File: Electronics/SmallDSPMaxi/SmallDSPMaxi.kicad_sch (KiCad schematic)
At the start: 103 parts, among them J1 Header, J10 Header, J11 Programming, J2 Header, J3 Header, J4 Header, J5 Header, J6 Header, J7 Header, J8 Header, J9 Header, Q1 NSS1C300ET4G, SW1 SW_4PDT, SW2 TS-1187A-B-A-B, U1 ADAU1467, U2 ADM811, U3 M95M01-R, Y1 830105957509

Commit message: Adds final state of Maxi rev 1.0 and unbalanced IO boards rev 1.0.
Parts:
- removed D1, D10, D11, D12, D2, D3, D4, D5, D6, D7, D8, D9: P6SMB6.8CA, Diode_SMD:D_SMB, symbol Device:D_TVS
- added JP1: SolderJumper_2_Open, Jumper:SolderJumper-2_P1.3mm_Open_RoundedPad1.0x1.5mm, symbol Jumper:SolderJumper_2_Open
- added TP?: TestPoint, TestPoint:TestPoint_Pad_D1.0mm, symbol Connector:TestPoint_Small
- added U1, U3, U4: H5VU25U, Package_DFN_QFN:Diodes_UDFN-10_1.0x2.5mm_P0.5mm, symbol 1_Project_Symbols:H5VU25U
- U2: renamed from U1; Part Number ADAU1463 -> ADAU1467WBCPZ300
- Y1: Assembling (none) -> X
- renumbered C2 to C1, C1 to C2, C4 to C3, C5 to C4, C7 to C5, C8 to C6, C6 to C7, C3 to C8, D13 to D1, J9 to J10, J10 to J11, J11 to J7, J7 to J8, J8 to J9, R38 to R28, R33 to R32, R34 to R33, R28 to R34, R32 to R38, U1 to U2, U3 to U5, U2 to U6
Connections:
- net 5V PR: now also U3.4
- net Earth_Protective: now also U1.3 (VSS), U1.8 (VSS), U3.3 (VSS), U3.8 (VSS), U4.3 (VSS), U4.8 (VSS)
- net MCU SCL: now also U1.1
- net MCU SDA: now also U1.2
- net PRGM MISO: now also U3.5
- net PRGM MOSI: now also U4.2
- net PRGM SCLK: now also U3.2
- net ~{DSP RST}: now also JP1.2 (B)
- net ~{PRGM CS}: now also U3.1
- net at C2.1, R34.1, SW2.2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: now also JP1.1 (A), TP?.1, U4.4
- net at SW1.5 (B), TP?.1, U2.39 (S_SCL/S_SCLK): now also U1.4
- net at SW1.11 (B), U2.42 (Selfboot): now also U4.5
- net at SW1.2 (B), TP?.1, U2.38 (S_SDA/S_MISO): now also U1.5
- net BCLK In0 renamed DSP BCLK In 1
- net BCLK In1 renamed DSP BCLK In 2
- net BCLK In2 renamed DSP BCLK In 3
- net BCLK In3 renamed DSP BCLK In 4
- net BCLK Out0 renamed DSP BCLK Out 1
- net BCLK Out1 renamed DSP BCLK Out 2
- net BCLK Out2 renamed DSP BCLK Out 3
- net BCLK Out3 renamed DSP BCLK Out 4
- net GPIO14 renamed DSP GPIO14
- net GPIO15 renamed DSP GPIO15
- net GPIO6 renamed DSP GPIO6
- net GPIO7 renamed DSP GPIO7
- net LRCK In0 renamed DSP LRCK In 1
- net LRCK In1 renamed DSP LRCK In 2
- net LRCK In2 renamed DSP LRCK In 3
- net LRCK In3 renamed DSP LRCK In 4
- net LRCK Out0 renamed DSP LRCK Out 1
- net LRCK Out1 renamed DSP LRCK Out 2
- net LRCK Out2 renamed DSP LRCK Out 3
- net LRCK Out3 renamed DSP LRCK Out 4
- net M DSP MISO renamed DSP MISO
- net M DSP MOSI renamed DSP MOSI
- net M DSP SCLK renamed DSP SCLK
- net MCLK renamed DSP MCLK
- net SDATA In0 renamed DSP I²S SDI 1
- net SDATA In1 renamed DSP I²S SDI 2
- net SDATA In2 renamed DSP I²S SDI 3
- net SDATA In3 renamed DSP I²S SDI 4
- net SDATA In4 renamed DSP I²S SDI 5
- net SDATA In5 renamed DSP I²S SDI 6
- net SDATA In6 renamed DSP I²S SDI 7
- net SDATA In7 renamed DSP I²S SDI 8
- net SDATA Out0 renamed DSP I²S SDO 1
- net SDATA Out1 renamed DSP I²S SDO 2
- net SDATA Out2 renamed DSP I²S SDO 3
- net SDATA Out3 renamed DSP I²S SDO 4
- net SDATA Out4 renamed DSP I²S SDO 5
- net SDATA Out5 renamed DSP I²S SDO 6
- net SDATA Out6 renamed DSP I²S SDO 7
- net SDATA Out7 renamed DSP I²S SDO 8
- net ~{RST MCU} renamed ~{DSP RST MCU}
- net ~{RST PGRM} renamed ~{DSP RST PGRM}
- net ~{DSP RST PGRM}: now also U4.1
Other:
- moved on the sheet: C1, C2, C3, C4, C5, C6, C7, C8, C9, D1, J1, J10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

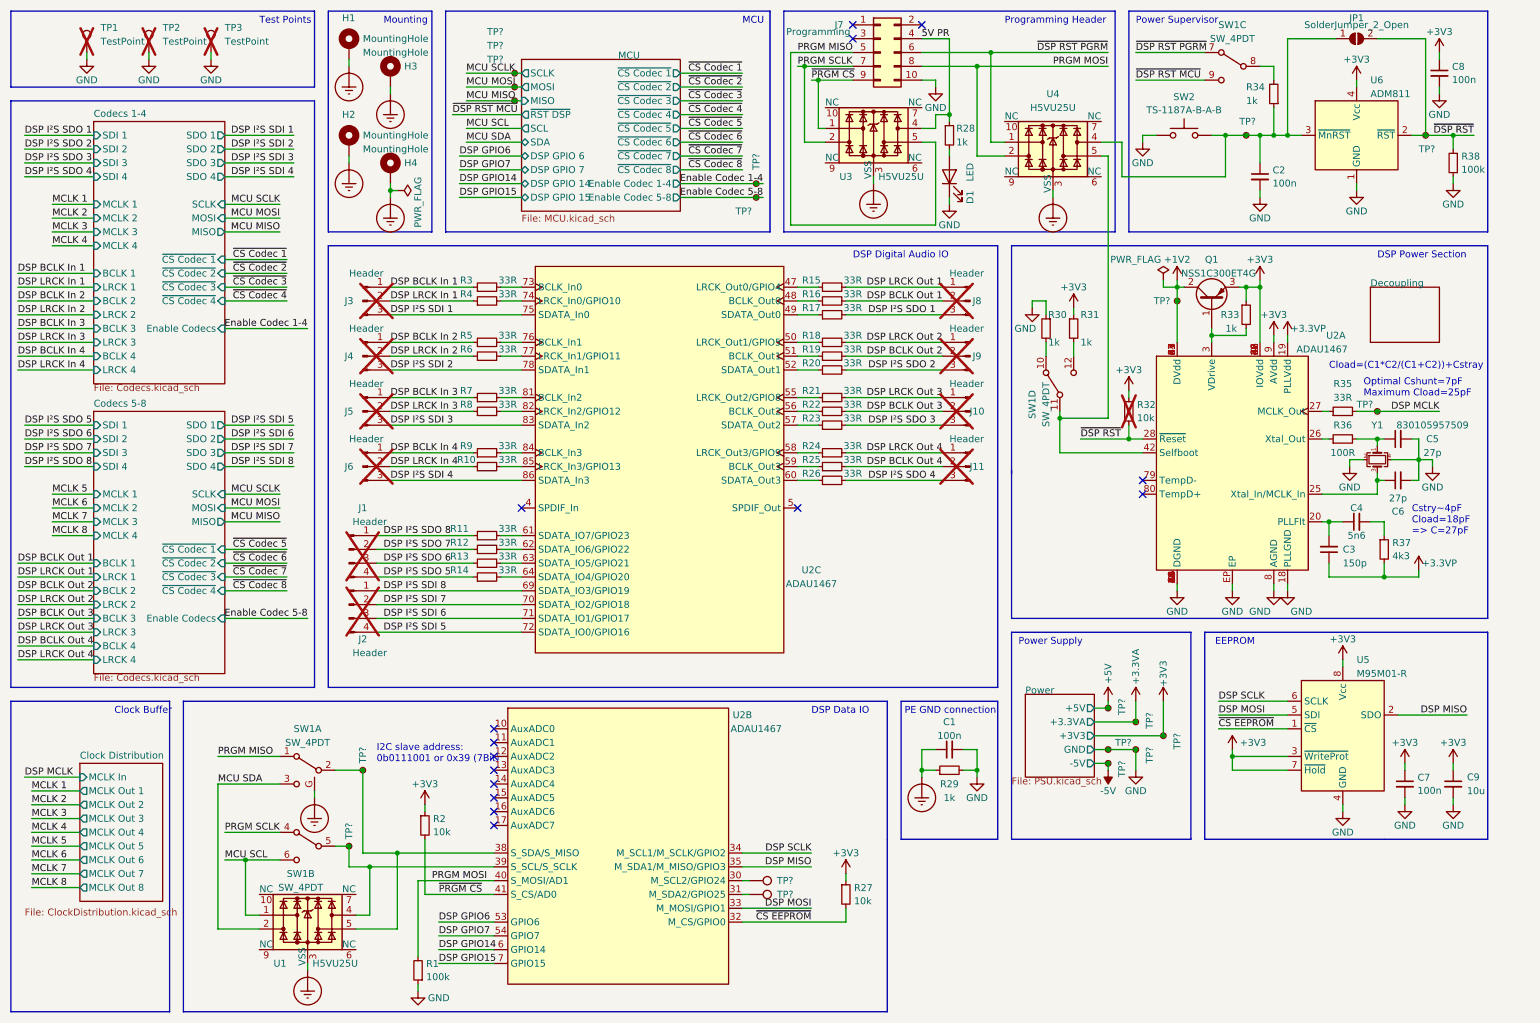
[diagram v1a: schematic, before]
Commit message: Maxi: Replaces STM32 programming pin header with WE RedFit connectorand fixes minor issues. Adds driver for AKM AK4619 Codec and STM32CubeIDE workspace for Maxi firmware.
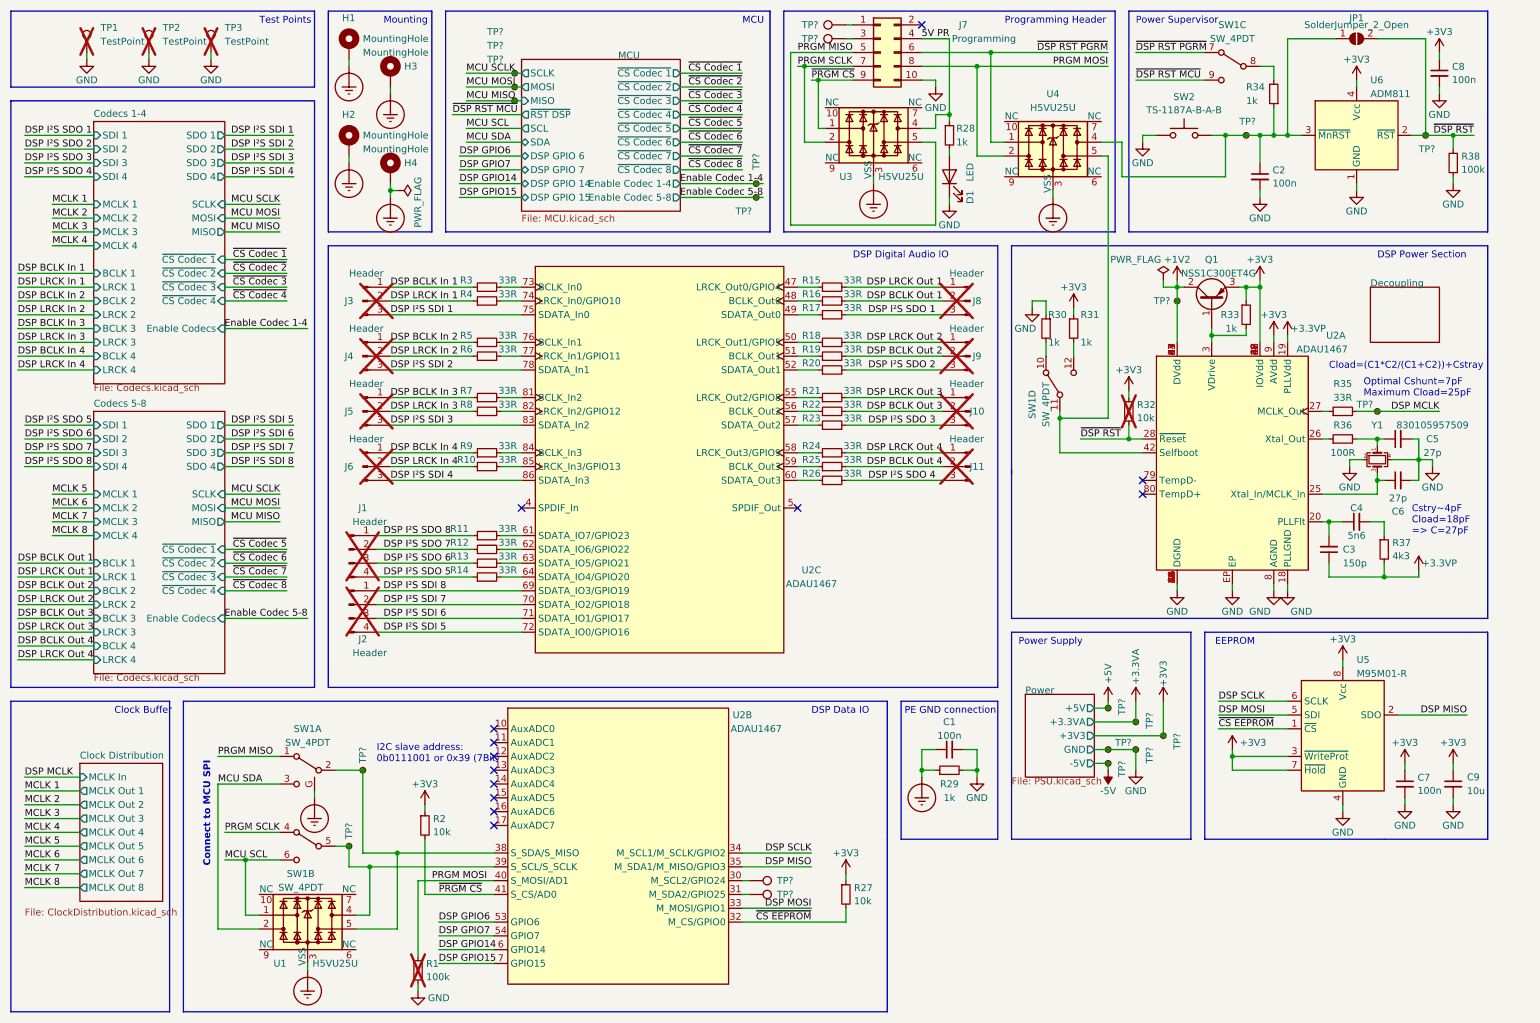
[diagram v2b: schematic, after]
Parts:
- added TP? (x2): TestPoint, TestPoint:TestPoint_Pad_D1.0mm, symbol Connector:TestPoint
- R1: now not fitted
- U2: LCSC Part # - -> C654415; Notes (none) -> Alterative: ADAU1463WBCPZ300RL (C654412) Less RAM.
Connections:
- net at J7.1 (Pin_1): now also TP?.1
- net at J7.3 (Pin_3): now also TP?.1
- no-connect marks 15 -> 13
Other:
- note added: "Connect to MCU SPI"

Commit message: Adds AES17 measurements for rev1 of maxi. adds first iteration of maxi firmware. prototype now functional. adds mechanical information such as pcb 3d models and datasheets for psu and power switch, -connector.
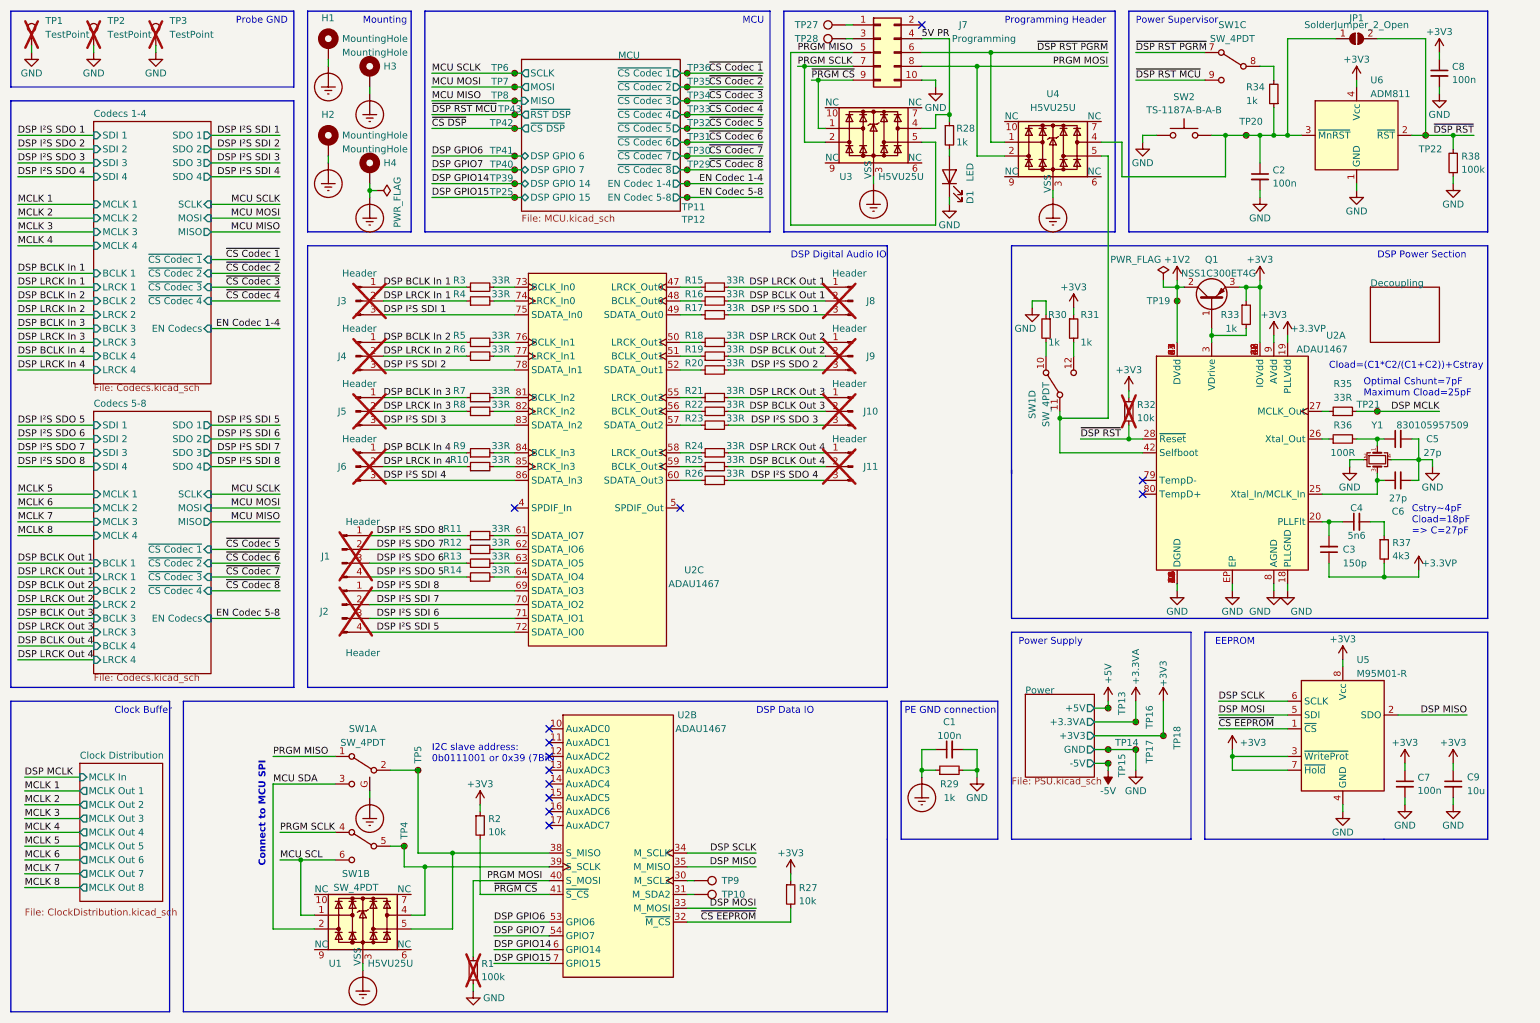
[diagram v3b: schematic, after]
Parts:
- added TP25, TP29, TP30, TP31, TP32, TP33, TP34, TP35, TP36, TP39, TP40, TP41, TP42, TP43: TestPoint, TestPoint:TestPoint_Pad_D1.0mm, symbol Connector:TestPoint_Small
- U2: Part Number ADAU1467WBCPZ300 -> ADAU1463
- gave numbers to parts that had none: 21
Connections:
- net DSP GPIO14: now also TP39.1
- net DSP GPIO15: now also TP25.1
- net DSP GPIO6: now also TP41.1
- net DSP GPIO7: now also TP40.1
- net ~{CS Codec 1}: now also TP36.1
- net ~{CS Codec 2}: now also TP35.1
- net ~{CS Codec 3}: now also TP34.1
- net ~{CS Codec 4}: now also TP33.1
- net ~{CS Codec 5}: now also TP32.1
- net ~{CS Codec 6}: now also TP31.1
- net ~{CS Codec 7}: now also TP30.1
- net ~{CS Codec 8}: now also TP29.1
- net ~{DSP RST MCU}: now also TP43.1
- net Enable Codec 1-4 renamed EN Codec 1-4
- net Enable Codec 5-8 renamed EN Codec 5-8
- new net ~{CS DSP}: TP42.1
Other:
- sheet Codecs 1-4 ports: added EN Codecs; removed Enable Codecs
- sheet Codecs 5-8 ports: added EN Codecs; removed Enable Codecs
- sheet MCU ports: added EN Codec 1-4, EN Codec 5-8, ~{CS DSP}; removed Enable Codec 1-4, Enable Codec 5-8, SCL, SDA
- note added: "Probe GND"
- note removed: "Test Points"
- moved on the sheet: H1, H2, H3, H4, J1, J10, J11, J2, J3, J4, J5, J6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
